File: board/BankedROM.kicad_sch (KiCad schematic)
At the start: 16 parts, among them U28 AT29C040, U29 AT29C040, U30 AT29C040, U31 AT29C040, U32 AT29C040, U33 AT29C040, U34 AT29C040, U35 AT29C040

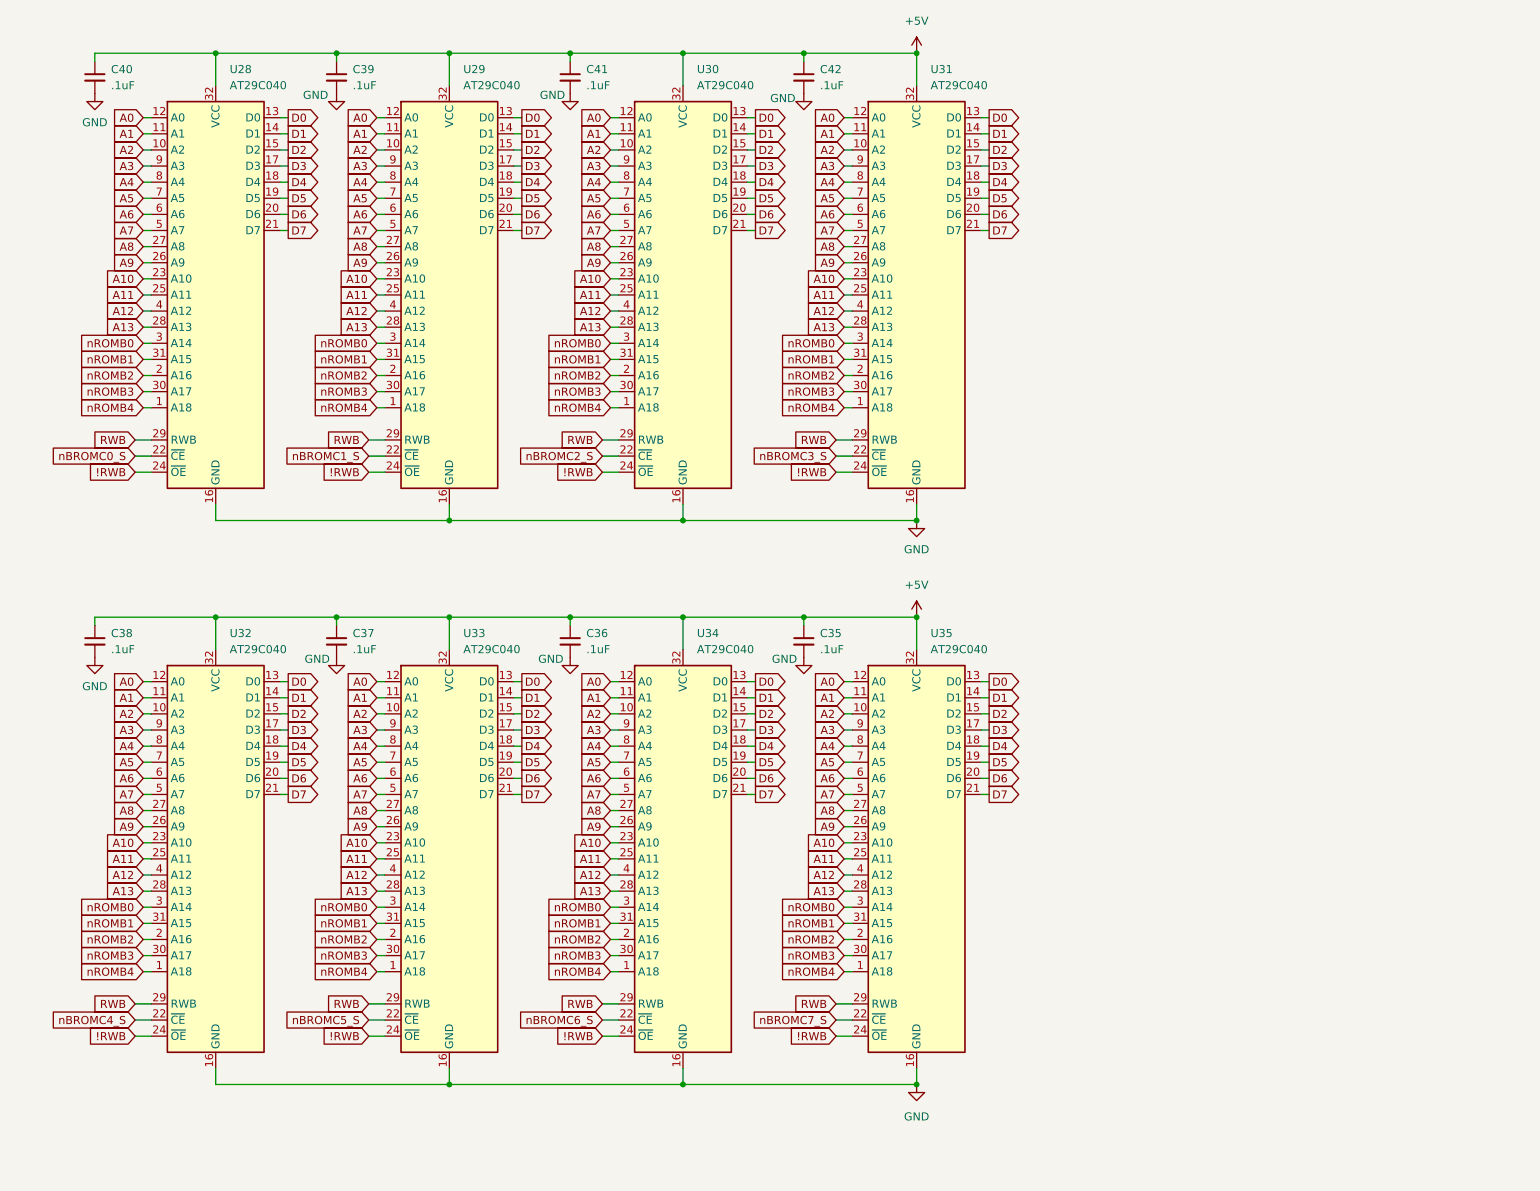
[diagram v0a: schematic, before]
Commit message: More main PCB updates.  Rearranged some things.  Bypass caps near PS connector.  Moved front panel connector to opposite side of board.
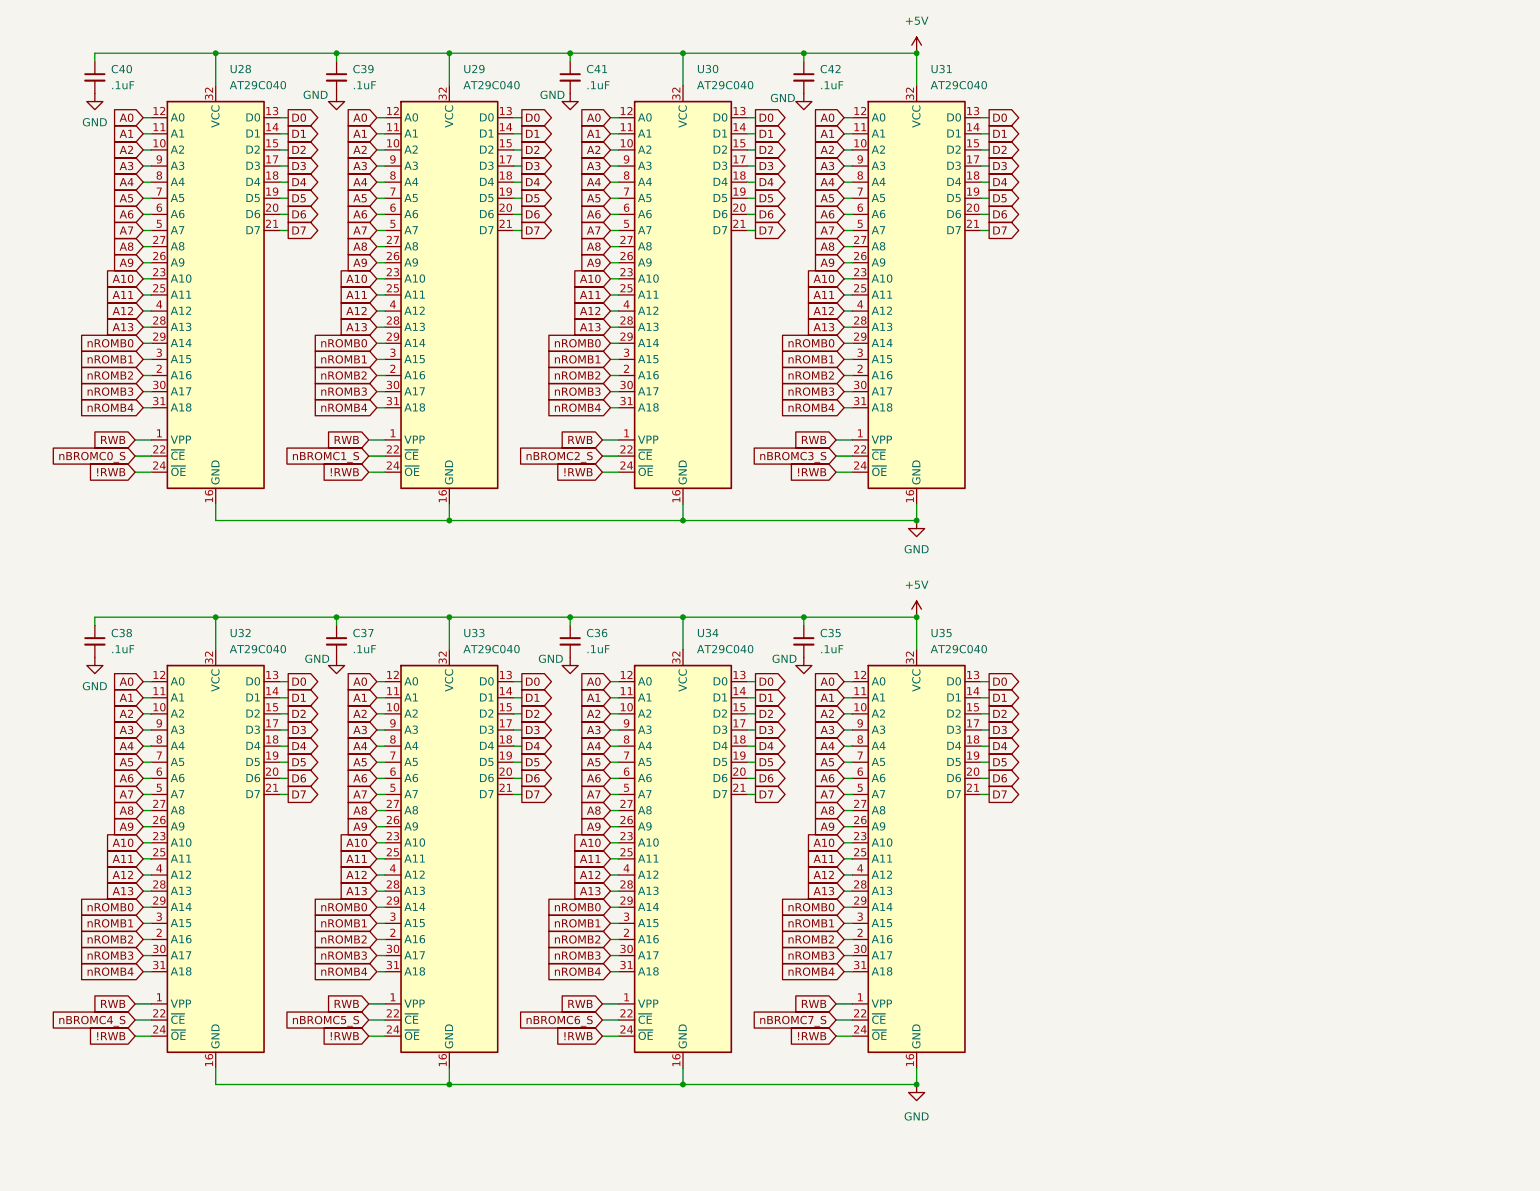
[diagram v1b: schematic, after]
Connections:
- net RWB: now also U28.1 (VPP), U29.1 (VPP), U30.1 (VPP), U31.1 (VPP), U32.1 (VPP), U33.1 (VPP), U34.1 (VPP), U35.1 (VPP); no longer U28.29 (RWB), U29.29 (RWB), U30.29 (RWB), U31.29 (RWB), U32.29 (RWB), U33.29 (RWB), U34.29 (RWB), U35.29 (RWB)
- net nROMB0: now also U28.29 (A14), U29.29 (A14), U30.29 (A14), U31.29 (A14), U32.29 (A14), U33.29 (A14), U34.29 (A14), U35.29 (A14); no longer U28.3 (A14), U29.3 (A14), U30.3 (A14), U31.3 (A14), U32.3 (A14), U33.3 (A14), U34.3 (A14), U35.3 (A14)
- net nROMB1: now also U28.3 (A15), U29.3 (A15), U30.3 (A15), U31.3 (A15), U32.3 (A15), U33.3 (A15), U34.3 (A15), U35.3 (A15); no longer U28.31 (A15), U29.31 (A15), U30.31 (A15), U31.31 (A15), U32.31 (A15), U33.31 (A15), U34.31 (A15), U35.31 (A15)
- net nROMB4: now also U28.31 (A18), U29.31 (A18), U30.31 (A18), U31.31 (A18), U32.31 (A18), U33.31 (A18), U34.31 (A18), U35.31 (A18); no longer U28.1 (A18), U29.1 (A18), U30.1 (A18), U31.1 (A18), U32.1 (A18), U33.1 (A18), U34.1 (A18), U35.1 (A18)
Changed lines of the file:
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@@
 			)
 		)
-		(property "Datasheet" ""
+		(property "Datasheet" "http://ww1.microchip.com/downloads/en/devicedoc/doc0189.pdf"
 			(at 48.26 148.59 0)
 			(effects
@@
 			)
 		)
-		(property "Description" "Atmel Flash 4 MiBit (512 Ki x 8)"
+		(property "Description" "OTP EPROM 4 MiBit (512 Ki x 8)"
 			(at 48.26 148.59 0)
 			(effects
@@
 			)
 		)
-		(property "Datasheet" ""
+		(property "Datasheet" "http://ww1.microchip.com/downloads/en/devicedoc/doc0189.pdf"
 			(at 48.26 59.69 0)
 			(effects
@@
 			)
 		)
-		(property "Description" "Atmel Flash 4 MiBit (512 Ki x 8)"
+		(property "Description" "OTP EPROM 4 MiBit (512 Ki x 8)"
 			(at 48.26 59.69 0)
 			(effects
@@
 			)
 		)
-		(property "Datasheet" ""
+		(property "Datasheet" "http://ww1.microchip.com/downloads/en/devicedoc/doc0189.pdf"
 			(at 85.09 59.69 0)
 			(effects
@@
 			)
 		)
-		(property "Description" "Atmel Flash 4 MiBit (512 Ki x 8)"
+		(property "Description" "OTP EPROM 4 MiBit (512 Ki x 8)"
 			(at 85.09 59.69 0)
 			(effects
@@
 			)
 		)
-		(property "Datasheet" ""
+		(property "Datasheet" "http://ww1.microchip.com/downloads/en/devicedoc/doc0189.pdf"
 			(at 85.09 148.59 0)
 			(effects
@@
 			)
 		)
-		(property "Description" "Atmel Flash 4 MiBit (512 Ki x 8)"
+		(property "Description" "OTP EPROM 4 MiBit (512 Ki x 8)"
 			(at 85.09 148.59 0)
 			(effects
@@
 			)
 		)
-		(property "Datasheet" ""
+		(property "Datasheet" "http://ww1.microchip.com/downloads/en/devicedoc/doc0189.pdf"
 			(at 158.75 59.69 0)
 			(effects
@@
 			)
 		)
-		(property "Description" "Atmel Flash 4 MiBit (512 Ki x 8)"
+		(property "Description" "OTP EPROM 4 MiBit (512 Ki x 8)"
 			(at 158.75 59.69 0)
 			(effects
@@
 			)
 		)
-		(property "Datasheet" ""
+		(property "Datasheet" "http://ww1.microchip.com/downloads/en/devicedoc/doc0189.pdf"
 			(at 158.75 148.59 0)
 			(effects
@@
 			)
 		)
-		(property "Description" "Atmel Flash 4 MiBit (512 Ki x 8)"
+		(property "Description" "OTP EPROM 4 MiBit (512 Ki x 8)"
 			(at 158.75 148.59 0)
 			(effects
@@
 			)
 		)
-		(property "Datasheet" ""
+		(property "Datasheet" "http://ww1.microchip.com/downloads/en/devicedoc/doc0189.pdf"
 			(at 121.92 59.69 0)
 			(effects
@@
 			)
 		)
-		(property "Description" "Atmel Flash 4 MiBit (512 Ki x 8)"
+		(property "Description" "OTP EPROM 4 MiBit (512 Ki x 8)"
 			(at 121.92 59.69 0)
 			(effects
@@
 			)
 		)
-		(property "Datasheet" ""
+		(property "Datasheet" "http://ww1.microchip.com/downloads/en/devicedoc/doc0189.pdf"
 			(at 121.92 148.59 0)
 			(effects
@@
 			)
 		)
-		(property "Description" "Atmel Flash 4 MiBit (512 Ki x 8)"
+		(property "Description" "OTP EPROM 4 MiBit (512 Ki x 8)"
 			(at 121.92 148.59 0)
 			(effects

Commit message: Schematic Bus updates, silkscreen updates, position tweaks, and other corrections.
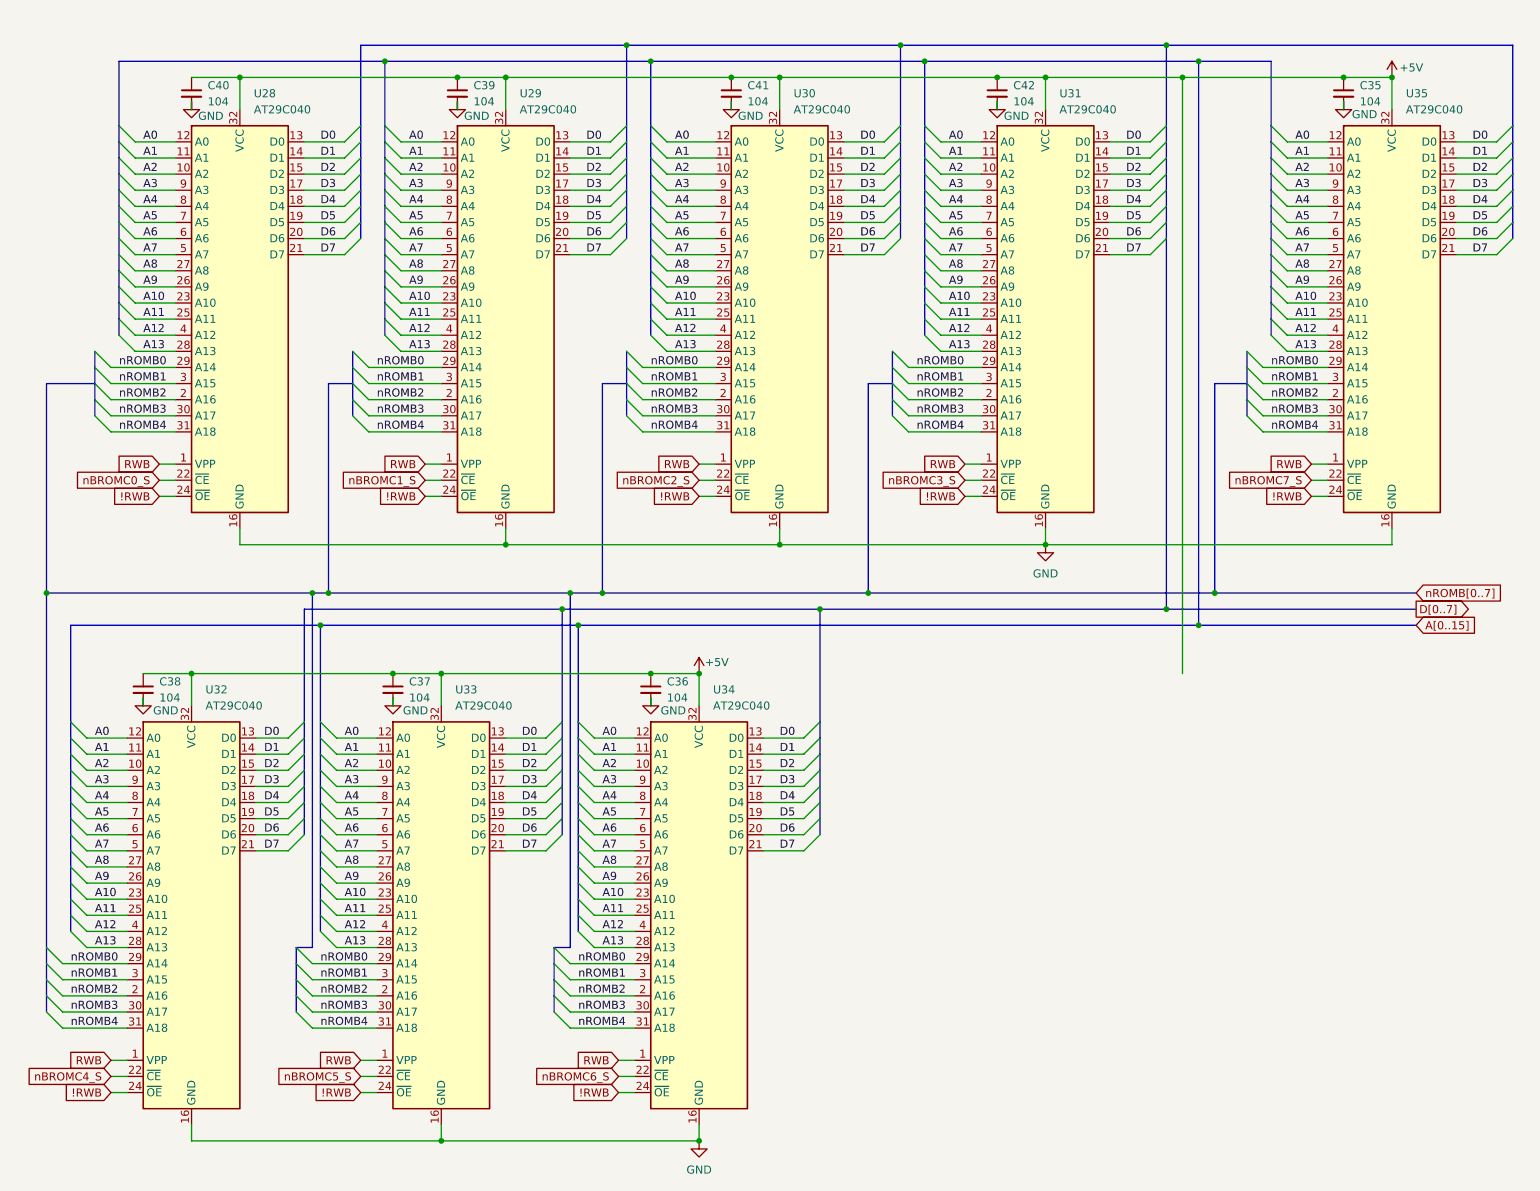
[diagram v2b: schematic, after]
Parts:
- C35, C36, C37, C38, C39, C40, C41, C42: value .1uF -> 104
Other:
- company: (none) -> Data Tuning
- title: Banked ROM -> Shared ROM Banks
- moved on the sheet: C36, C37, C38, C39, C40, C41, C42, U28, U29, U30, U31, U32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

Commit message: Fixing A9 routing on main schematic, and adding new footprint for the DSUB-9 serial connector.
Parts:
- C40: footprint Capacitor_THT:C_Disc_D4.3mm_W1.9mm_P5.00mm -> Capacitor_THT:C_Disc_D5.0mm_W2.5mm_P5.00mm
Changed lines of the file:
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@@
 	(title_block
 		(title "Shared ROM Banks")
-		(date "2024-10-09")
-		(rev "0.3B")
+		(date "2024-10-21")
+		(rev "0.4A")
 		(company "Data Tuning")
 		(comment 1 "Hydra 16")
@@
 			)
 		)
-		(property "Footprint" "Capacitor_THT:C_Disc_D4.3mm_W1.9mm_P5.00mm"
+		(property "Footprint" "Capacitor_THT:C_Disc_D5.0mm_W2.5mm_P5.00mm"
 			(at 44.45 27.94 0)
 			(effects

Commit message: Board version 0.6F, moving stuff around and updating the silkscreen to be more consistent.
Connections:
- net nROMB0 renamed ROMB0
- net nROMB1 renamed ROMB1
- net nROMB2 renamed ROMB2
- net nROMB3 renamed ROMB3
- net nROMB4 renamed ROMB4
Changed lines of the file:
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@@
 	(title_block
 		(title "Shared ROM Banks")
-		(date "2024-10-21")
-		(rev "0.5A")
+		(date "2024-11-21")
+		(rev "0.5C")
 		(company "Data Tuning")
 		(comment 1 "Hydra 16")
@@
 		)
 	)
-	(label "nROMB2"
+	(label "ROMB2"
 		(at 33.02 76.2 0)
 		(fields_autoplaced yes)
@@
 		)
 	)
-	(label "nROMB4"
+	(label "ROMB4"
 		(at 64.77 175.26 0)
 		(fields_autoplaced yes)
@@
 		)
 	)
-	(label "nROMB1"
+	(label "ROMB1"
 		(at 158.75 73.66 0)
 		(fields_autoplaced yes)
@@
 		)
 	)
-	(label "nROMB2"
+	(label "ROMB2"
 		(at 73.66 76.2 0)
 		(fields_autoplaced yes)
@@
 		)
 	)
-	(label "nROMB3"
+	(label "ROMB3"
 		(at 25.4 172.72 0)
 		(fields_autoplaced yes)
@@
 		)
 	)
-	(label "nROMB3"
+	(label "ROMB3"
 		(at 105.41 172.72 0)
 		(fields_autoplaced yes)
@@
 		)
 	)
-	(label "nROMB2"
+	(label "ROMB2"
 		(at 105.41 170.18 0)
 		(fields_autoplaced yes)
@@
 		)
 	)
-	(label "nROMB3"
+	(label "ROMB3"
 		(at 33.02 78.74 0)
 		(fields_autoplaced yes)
@@
 		)
 	)
-	(label "nROMB4"
+	(label "ROMB4"
 		(at 73.66 81.28 0)
 		(fields_autoplaced yes)
@@
 		)
 	)
-	(label "nROMB1"
+	(label "ROMB1"
 		(at 214.63 73.66 0)
 		(fields_autoplaced yes)
@@
 		)
 	)
-	(label "nROMB3"
+	(label "ROMB3"
 		(at 214.63 78.74 0)
 		(fields_autoplaced yes)
@@
 		)
 	)
-	(label "nROMB1"
+	(label "ROMB1"
 		(at 64.77 167.64 0)
 		(fields_autoplaced yes)
@@
 		)
 	)
-	(label "nROMB1"
+	(label "ROMB1"
 		(at 25.4 167.64 0)
 		(fields_autoplaced yes)
@@
 		)
 	)
-	(label "nROMB2"
+	(label "ROMB2"
 		(at 158.75 76.2 0)
 		(fields_autoplaced yes)
@@
 		)
 	)
-	(label "nROMB1"
+	(label "ROMB1"
 		(at 105.41 167.64 0)
 		(fields_autoplaced yes)
@@
 		)
 	)
-	(label "nROMB1"
+	(label "ROMB1"
 		(at 33.02 73.66 0)
 		(fields_autoplaced yes)
@@
 		)
 	)
-	(label "nROMB0"
+	(label "ROMB0"
 		(at 158.75 71.12 0)
 		(fields_autoplaced yes)
@@
 		)
 	)
-	(label "nROMB2"
+	(label "ROMB2"
 		(at 116.84 76.2 0)
 		(fields_autoplaced yes)
@@
 		)
 	)
-	(label "nROMB4"
+	(label "ROMB4"
 		(at 158.75 81.28 0)
 		(fields_autoplaced yes)
@@
 		)
 	)
-	(label "nROMB0"
+	(label "ROMB0"
 		(at 116.84 71.12 0)
 		(fields_autoplaced yes)
@@
 		)
 	)
-	(label "nROMB0"
+	(label "ROMB0"
 		(at 214.63 71.12 0)
 		(fields_autoplaced yes)
@@
 		)
 	)
-	(label "nROMB3"
+	(label "ROMB3"
 		(at 73.66 78.74 0)
 		(fields_autoplaced yes)
@@
 		)
 	)
-	(label "nROMB3"
+	(label "ROMB3"
 		(at 158.75 78.74 0)
 		(fields_autoplaced yes)
@@
 		)
 	)
-	(label "nROMB0"
+	(label "ROMB0"
 		(at 25.4 165.1 0)
 		(fields_autoplaced yes)
@@
 		)
 	)
-	(label "nROMB1"
+	(label "ROMB1"
 		(at 116.84 73.66 0)
 		(fields_autoplaced yes)
@@
 		)
 	)
-	(label "nROMB1"
+	(label "ROMB1"
 		(at 73.66 73.66 0)
 		(fields_autoplaced yes)
@@
 		)
 	)
-	(label "nROMB2"
+	(label "ROMB2"
 		(at 64.77 170.18 0)
 		(fields_autoplaced yes)
@@
 		)
 	)
-	(label "nROMB2"
+	(label "ROMB2"
 		(at 214.63 76.2 0)
 		(fields_autoplaced yes)
@@
 		)
 	)
-	(label "nROMB0"
+	(label "ROMB0"
 		(at 73.66 71.12 0)
 		(fields_autoplaced yes)
@@
 		)
 	)
-	(label "nROMB4"
+	(label "ROMB4"
 		(at 105.41 175.26 0)
 		(fields_autoplaced yes)
@@
 		)
 	)
-	(label "nROMB0"
+	(label "ROMB0"
 		(at 64.77 165.1 0)
 		(fields_autoplaced yes)
@@
 		)
 	)
-	(label "nROMB4"
+	(label "ROMB4"
 		(at 116.84 81.28 0)
 		(fields_autoplaced yes)
@@
 		)
 	)
-	(label "nROMB0"
+	(label "ROMB0"
 		(at 33.02 71.12 0)
 		(fields_autoplaced yes)
@@
 		)
 	)
-	(label "nROMB4"
+	(label "ROMB4"
 		(at 33.02 81.28 0)
 		(fields_autoplaced yes)
@@
 		)
 	)
-	(label "nROMB2"
+	(label "ROMB2"
 		(at 25.4 170.18 0)
 		(fields_autoplaced yes)
@@
 		)
 	)
-	(label "nROMB3"
+	(label "ROMB3"
 		(at 116.84 78.74 0)
 		(fields_autoplaced yes)
@@
 		)
 	)
-	(label "nROMB3"
+	(label "ROMB3"
 		(at 64.77 172.72 0)
 		(fields_autoplaced yes)
@@
 		)
 	)
-	(label "nROMB0"
+	(label "ROMB0"
 		(at 105.41 165.1 0)
 		(fields_autoplaced yes)
@@
 		)
 	)
-	(label "nROMB4"
+	(label "ROMB4"
 		(at 214.63 81.28 0)
 		(fields_autoplaced yes)
@@
 		)
 	)
-	(label "nROMB4"
+	(label "ROMB4"
 		(at 25.4 175.26 0)
 		(fields_autoplaced yes)
@@
 		)
 	)
-	(global_label "nROMB[0..7]"
+	(global_label "ROMB[0..7]"
 		(shape input)
 		(at 237.49 106.68 0)
@@
 		)
 		(property "Intersheetrefs" "${INTERSHEET_REFS}"
-			(at 226.8244 106.68 0)
+			(at 251.1191 106.68 0)
 			(effects
 				(font
 					(size 1.27 1.27)
 				)
-				(justify right)
+				(justify left)
 				(hide yes)
 			)
